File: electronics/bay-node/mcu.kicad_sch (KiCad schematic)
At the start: 15 parts, among them SW1 RESET, SW2 BOOT, U3 ESP32-S3-MINI-1-N8

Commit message: Bay node v0.5: 6-pin row cable with CAN and POS
The row cable becomes the docs/can.md contract: J1 (ROW IN, left) and J2 (ROW OUT,
right) are 6-pin JST PH S6B-PH-SM4-TB, +24 V, GND, CAN_H, CAN_L, GND, POS, with
pin 1 to the rear on the left edge and to the front on the right edge.

- Rack bus sheet: TCAN1044AV (VCC 5 V, VIO 3.3 V, STB low) right on the pair,
  which runs straight J1 -> J2 with no termination (stubs 1.8 / 2.3 mm),
  PESD2CAN on the tap; POS in through 10k + BAT54S + 100k pull-down, POS out
  through 10k + BAT54S.  TWAI on IO18/IO17, POS on IO16 (in) and IO35 (out).
- The input stage also takes a 20 / 28 V USB-C PD supply (notes on the Power
  sheet and in docs/electronics.md).
- Re-placed for In2 power only and autorouted: ERC 0, DRC 0, unconnected 0,
  parity 0 (kicad-cli and Konnect); no track on In1 or In2.
- JLC_CPL_FIX gains the rack bus parts, fitted on the EasyEDA footprints:
  S6B 180 deg, TCAN1044AV 270 deg, PESD2CAN and BAT54S 180 deg (they also apply
  to the power hub's row connectors, transceiver and clamps).
- Firmware: hwtr,rack-bus binding, TWAI pinctrl and node in the bay_node
  devicetree, check_pinmap and the README table; DevKitC moves POS_OUT to IO21,
  StampS3 disables the bus.  bay_node, DevKitC and StampS3 builds pass.
- Mechanics: the cable windows in the tray walls and the ladders widen to
  17 mm for the PHR-6 plug.  The viewer and the notice draw a 6-wire jumper.
- BOM: 6-pin jumpers; JLC_SINCE_QUOTE adds rev 0.5's parts and three extended
  part types to the node's quoted order (indicative, re-quote).

Regenerated: KiCad project, fab outputs, renders, schematic PDF, viewer GLB,
tray and ladder STLs, parts.glb, rack.json, bom/*.

Co-Authored-By: Claude Opus 5.5 <noreply@anthropic.com>
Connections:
- net POS_IN: now reaches U3.20 (IO16)
- net CAN_RXD: now reaches U3.21 (IO17)
- net CAN_TXD: now reaches U3.22 (IO18)
- net POS_OUT: now reaches U3.31 (IO35)
- no-connect marks 22 -> 18
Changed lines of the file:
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@@
 	(title_block
 		(title "Bay node — ESP32-S3 module")
-		(rev "0.4")
+		(rev "0.5")
 		(company "hw-testing-rack")
 		(comment 1 "ESP32-S3 USB/IP host for one bay of the hw-testing-rack shelf")
 		(comment 2 "Generated from electronics/bay-node/design.py — edit the Python, then regenerate")
-		(comment 3 "24 V in · 5 V/1.4 A switched DUT port · USB 2.0 muxes · INA226 · AUX UART/RST/BOOT")
+		(comment 3 "Row bus 20–28 V + CAN + POS in/out · 5 V/1.4 A switched DUT port · USB 2.0 muxes · INA226 · AUX")
 	)
 	(symbol
@@
 		)
 	)
-	(no_connect
-		(at 187.96 116.84)
+	(wire
+		(pts
+			(xy 187.96 116.84)
+			(xy 185.42 116.84)
+		)
+		(stroke
+			(width 0)
+			(type default)
+		)
 	)
-	(no_connect
-		(at 187.96 119.38)
+	(global_label "POS_IN"
+		(shape bidirectional)
+		(at 185.42 116.84 180)
+		(fields_autoplaced yes)
+		(effects
+			(font
+				(size 1.27 1.27)
+			)
+			(justify right)
+		)
+		(property "Intersheetrefs" "${INTERSHEET_REFS}"
+			(at 185.42 116.84 0)
+			(effects
+				(font
+					(size 1.27 1.27)
+				)
+				(justify right)
+				(hide yes)
+			)
+		)
 	)
-	(no_connect
-		(at 187.96 121.92)
+	(wire
+		(pts
+			(xy 187.96 119.38)
+			(xy 185.42 119.38)
+		)
+		(stroke
+			(width 0)
+			(type default)
+		)
+	)
+	(global_label "CAN_RXD"
+		(shape bidirectional)
+		(at 185.42 119.38 180)
+		(fields_autoplaced yes)
+		(effects
+			(font
+				(size 1.27 1.27)
+			)
+			(justify right)
+		)
+		(property "Intersheetrefs" "${INTERSHEET_REFS}"
+			(at 185.42 119.38 0)
+			(effects
+				(font
+					(size 1.27 1.27)
+				)
+				(justify right)
+				(hide yes)
+			)
+		)
+	)
+	(wire
+		(pts
+			(xy 187.96 121.92)
+			(xy 185.42 121.92)
+		)
+		(stroke
+			(width 0)
+			(type default)
+		)
+	)
+	(global_label "CAN_TXD"
+		(shape bidirectional)
+		(at 185.42 121.92 180)
+		(fields_autoplaced yes)
+		(effects
+			(font
+				(size 1.27 1.27)
+			)
+			(justify right)
+		)
+		(property "Intersheetrefs" "${INTERSHEET_REFS}"
+			(at 185.42 121.92 0)
+			(effects
+				(font
+					(size 1.27 1.27)
+				)
+				(justify right)
+				(hide yes)
+			)
+		)
 	)
 	(wire
@@
 		)
 	)
-	(no_connect
-		(at 218.44 93.98)
+	(wire
+		(pts
+			(xy 218.44 93.98)
+			(xy 220.98 93.98)
+		)
+		(stroke
+			(width 0)
+			(type default)
+		)
+	)
+	(global_label "POS_OUT"
+		(shape bidirectional)
+		(at 220.98 93.98 0)
+		(fields_autoplaced yes)
+		(effects
+			(font
+				(size 1.27 1.27)
+			)
+			(justify left)
+		)
+		(property "Intersheetrefs" "${INTERSHEET_REFS}"
+			(at 220.98 93.98 0)
+			(effects
+				(font
+					(size 1.27 1.27)
+				)
+				(justify left)
+				(hide yes)
+			)
+		)
 	)
 	(no_connect
@@
 		)
 	)
-	(text_box "GPIO map: IO41 DUT_EN · IO40 DUT_FLT_N · IO39 INA_ALERT · IO38/37 I2C SDA/SCL · IO47/33 UART1 TX/RX (AUX) ·\nIO34 AUX_RST · IO48 AUX_BOOT · IO12 LED · IO13 PC_DET · IO14 MUX_FORCE_PC · IO15 SVC · IO19/20 USB (OTG/JTAG).\nStrapping pins IO0/IO3/IO45/IO46 are not used for I/O.  USB is full-speed only (one internal PHY)."
+	(text_box "GPIO map: IO41 DUT_EN · IO40 DUT_FLT_N · IO39 INA_ALERT · IO38/37 I2C SDA/SCL · IO47/33 UART1 TX/RX (AUX) ·\nIO34 AUX_RST · IO48 AUX_BOOT · IO12 LED · IO13 PC_DET · IO14 MUX_FORCE_PC · IO15 SVC · IO19/20 USB (OTG/JTAG) ·\nIO18/17 CAN TX/RX (TWAI) · IO16 POS_IN · IO35 POS_OUT.\nStrapping pins IO0/IO3/IO45/IO46 are not used for I/O.  USB is full-speed only (one internal PHY)."
 		(exclude_from_sim no)
 		(at 15.24 177.8 0)
-		(size 269.24 11.43)
+		(size 269.24 13.97)
 		(margins 1.5 1.5 1.5 1.5)
 		(stroke

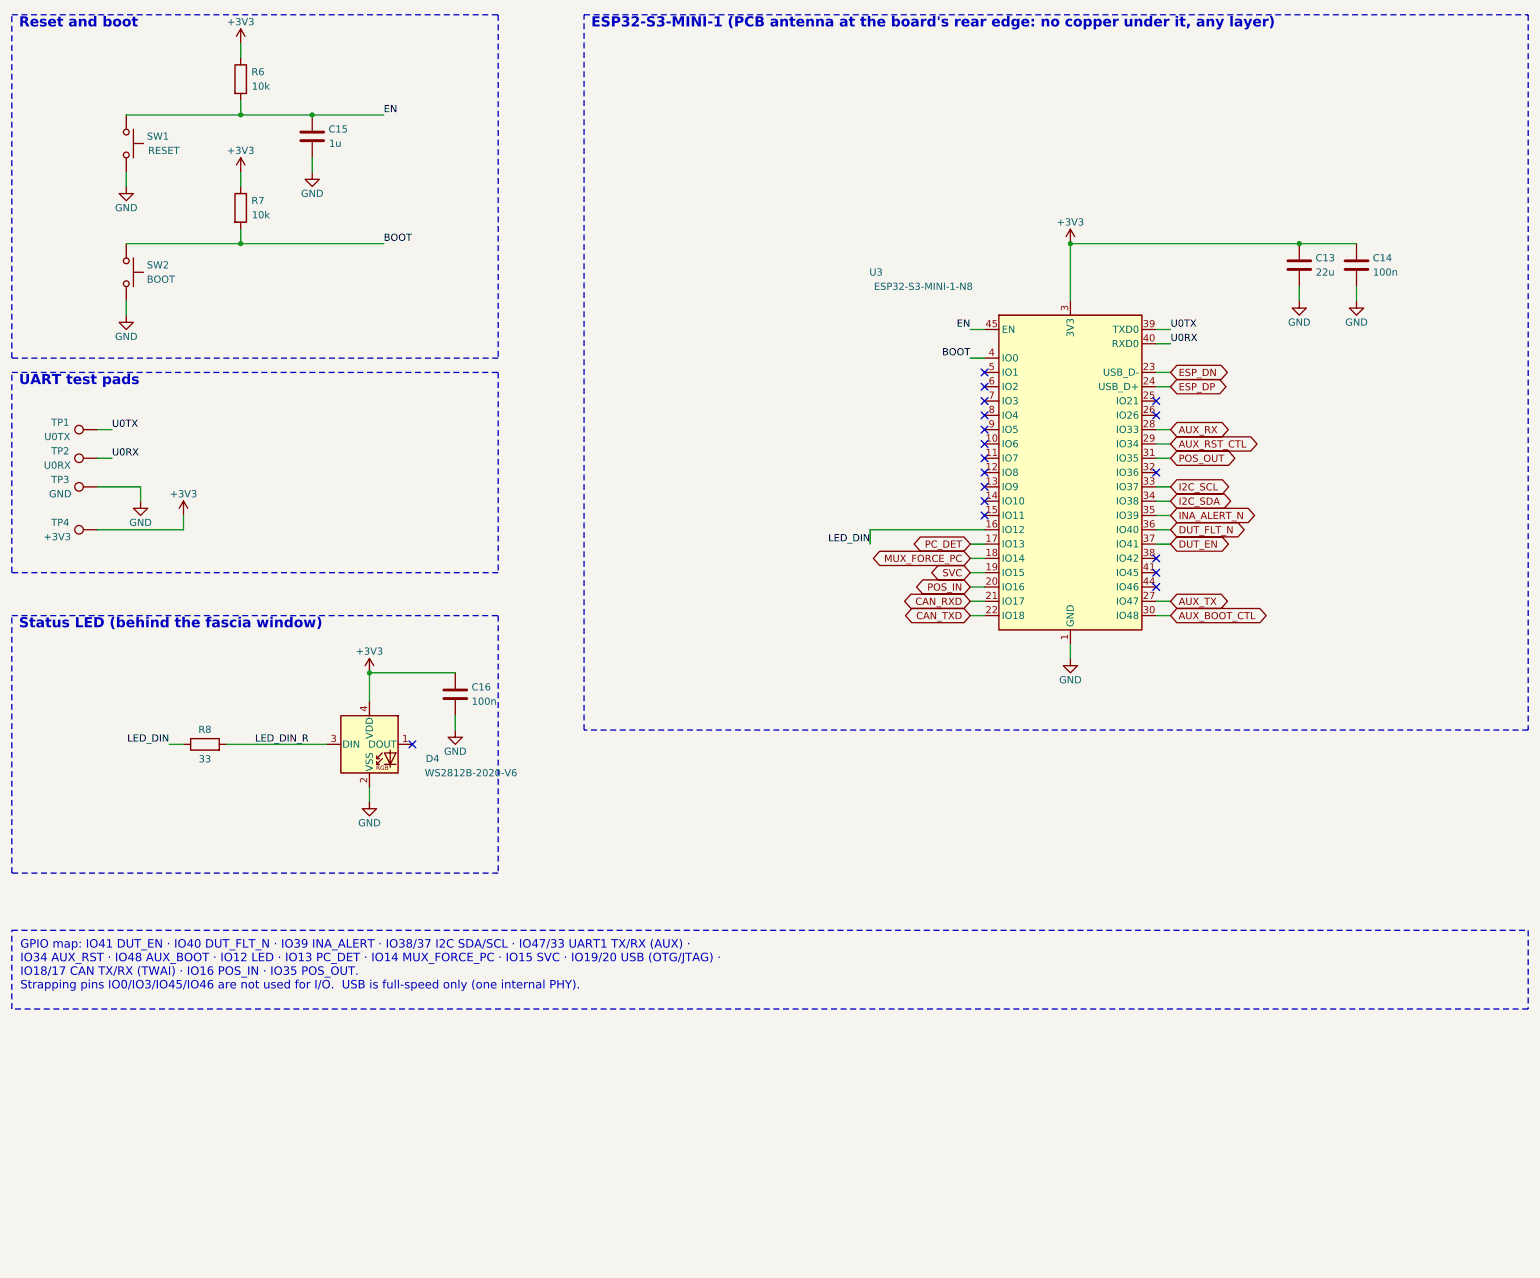
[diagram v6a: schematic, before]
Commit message: Bay node: the bay's camera on J6, the WROOM-1-N8R8, the board 64 × 90
The user chose a camera per bay wired to its own node (camera hand-over,
option B: an Arducam Mega 3MP SPI, M12 ≈ 120°, and white LEDs on one PH 8
lead) and the ESP32-S3-WROOM-1-N8R8 for its 8 MB octal PSRAM, allowing
the board to grow at the rear.

- U3: WROOM-1-N8R8 (C2913201), the DevKitC-1-N8R8's module.  The board
  grew 10 mm at the rear (64 × 90): the layout, the holes and every
  pcb.bay_node y moved 10 mm with it, so the tray's standoffs and the
  fascia parts keep their place; the module's top edge is the new rear
  edge, its antenna band (6 mm, ±24 mm) kept clear.  bench footprint
  ESP32-S3-WROOM-1_NoEPVias: the stock one without its 0.2 mm in-pad
  vias, the pad on a GND island stitched around it.
- Pin map (the PSRAM takes IO35–37, no IO26/33/34 on a WROOM-1), the
  DevKitC-1 v1.1's as is: IO1/IO2 I²C, IO12 AUX_RST, IO21 AUX_RX, IO38 LED,
  IO42 POS_OUT; camera IO11 SCK, IO10 MOSI, IO9 MISO, IO8 CS, IO7 light.
- J6: PH 8 vertical (B8B) right of the PC pair, under J7; 33 Ω series,
  2 × USBLC6, CS 10k pull-up, MISO divider footprint (R35 DNP), the light
  on an AO3400A (100k gate pull-down), CAM_5V through the PTC.  A
  "Camera" schematic sheet.
- J5 (AUX): a vertical PH 6 (B6B), as the user asked.
- Re-routed.  ERC 0, DRC 0 / 0 unconnected / parity 0, JLC DFM: only the
  back-side test pads, 97/97 3D models (the B6B's EasyEDA STEP is not
  centred and turned).  The session import now also drops a via at the
  end of a dead branch, and the branch.  JLC corrections fitted for
  C2913201, C495548, C471518, C20917.
- BOM: the camera lines (B0434, 120° lens, LED strip, PH 8 lead) replace
  the XIAO / OV2640 / PH 2 lead; the node's post-quote changes +$18.91
  of parts, +$3 for the B6B type, +$1.83 for the larger board.
- firmware/README.md pin map: the new map.  check_pinmap waits for the
  firmware's devicetree (moved pins, camera).

Co-Authored-By: Claude Opus 5.5 <noreply@anthropic.com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
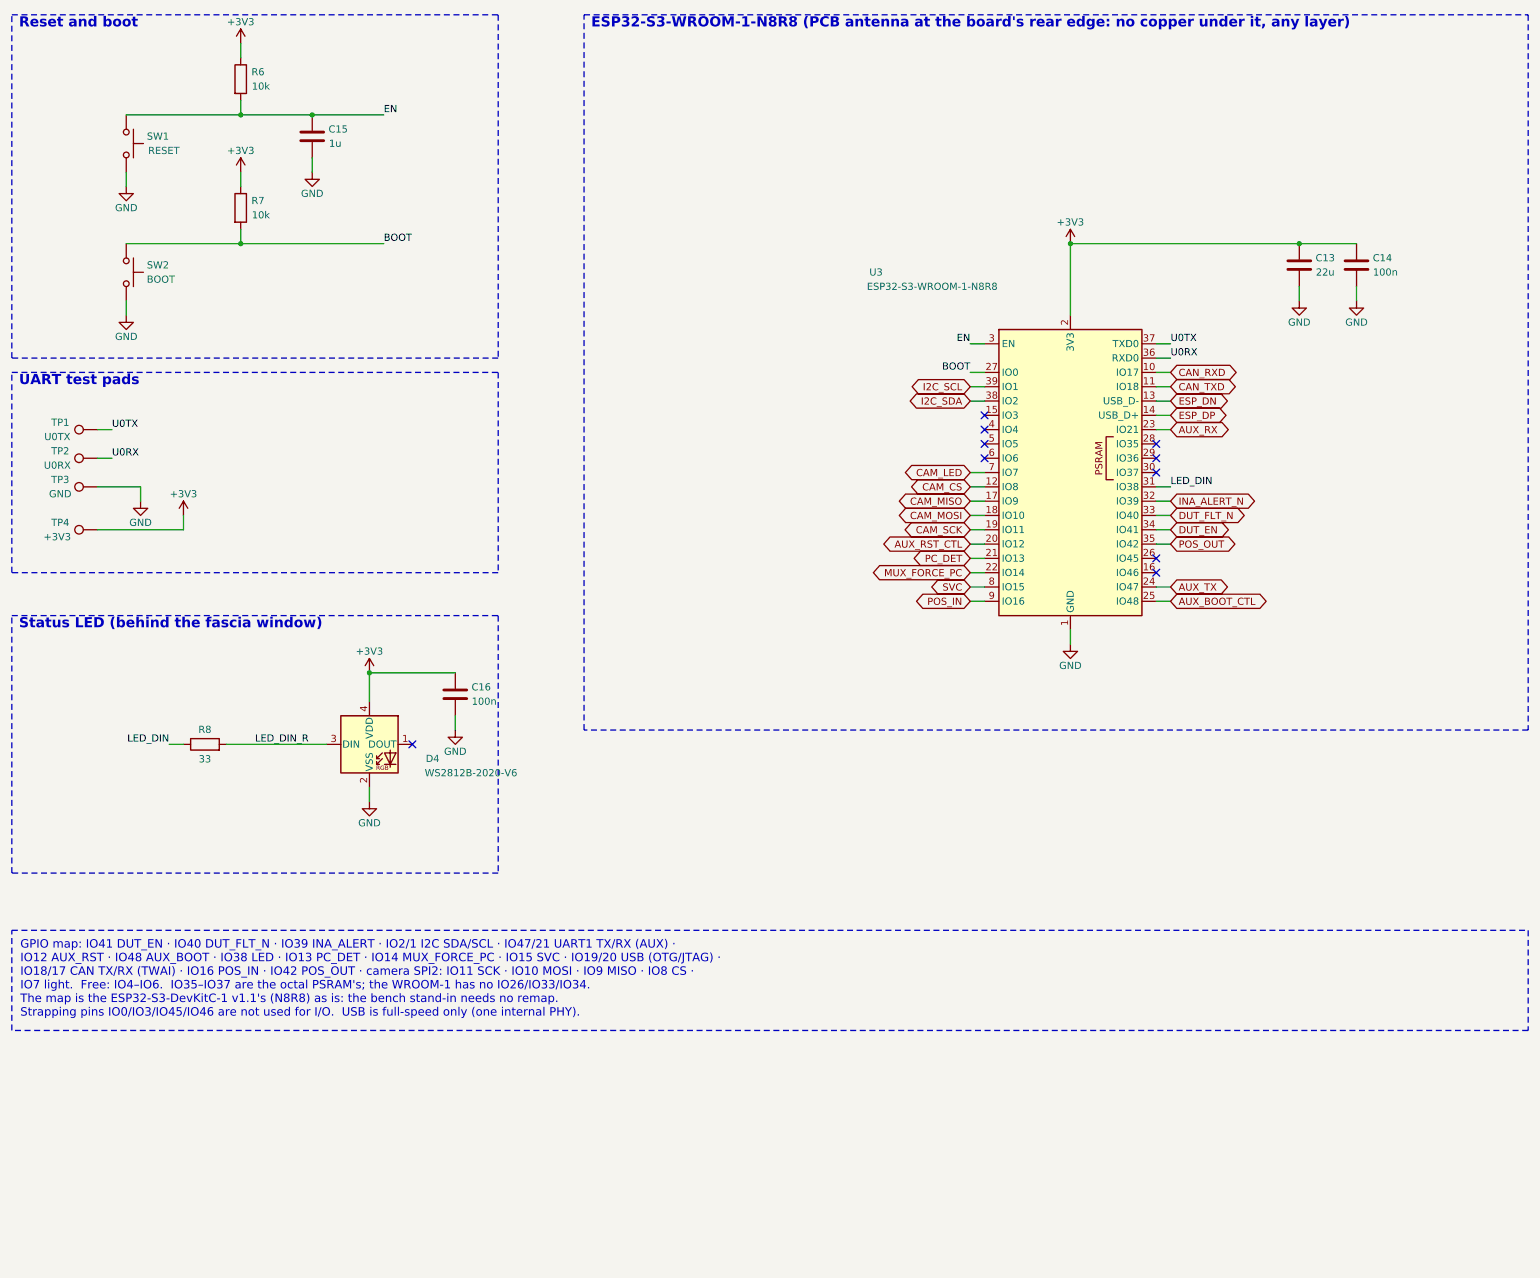
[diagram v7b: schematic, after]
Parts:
- U3: value ESP32-S3-MINI-1-N8 -> ESP32-S3-WROOM-1-N8R8; footprint RF_Module:ESP32-S2-MINI-1 -> bench:ESP32-S3-WROOM-1_NoEPVias; symbol RF_Module:ESP32-S3-MINI-1 -> RF_Module:ESP32-S3-WROOM-1; LCSC C2913206 -> C2913201; MPN ESP32-S3-MINI-1-N8 -> ESP32-S3-WROOM-1-N8R8
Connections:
- net +3V3: now also U3.2 (3V3); no longer U3.3 (3V3)
- net AUX_BOOT_CTL: now also U3.25 (IO48); no longer U3.30 (IO48)
- net AUX_RST_CTL: now also U3.20 (IO12); no longer U3.29 (IO34)
- net AUX_RX: now also U3.23 (IO21); no longer U3.28 (IO33)
- net AUX_TX: now also U3.24 (IO47); no longer U3.27 (IO47)
- net BOOT: now also U3.27 (IO0); no longer U3.4 (IO0)
- net CAN_RXD: now also U3.10 (IO17); no longer U3.21 (IO17)
- net CAN_TXD: now also U3.11 (IO18); no longer U3.22 (IO18)
- net DUT_EN: now also U3.34 (IO41); no longer U3.37 (IO41)
- net DUT_FLT_N: now also U3.33 (IO40); no longer U3.36 (IO40)
- net EN: now also U3.3 (EN); no longer U3.45 (EN)
- net ESP_DN: now also U3.13 (USB_D-); no longer U3.23 (USB_D-)
- net ESP_DP: now also U3.14 (USB_D+); no longer U3.24 (USB_D+)
- net GND: now also U3.40 (GND), U3.41 (GND); no longer U3.2 (GND), U3.42 (GND), U3.43 (GND), U3.46 (GND), U3.47 (GND), U3.48 (GND), U3.49 (GND), U3.50 (GND), U3.51 (GND), U3.52 (GND), U3.53 (GND), U3.54 (GND), U3.55 (GND), U3.56 (GND), U3.57 (GND), U3.58 (GND), U3.59 (GND), U3.60 (GND), U3.61 (GND), U3.62 (GND), U3.63 (GND), U3.64 (GND), U3.65 (GND)
- net I2C_SCL: now also U3.39 (IO1); no longer U3.33 (IO37)
- net I2C_SDA: now also U3.38 (IO2); no longer U3.34 (IO38)
- net INA_ALERT_N: now also U3.32 (IO39); no longer U3.35 (IO39)
- net LED_DIN: now also U3.31 (IO38); no longer U3.16 (IO12)
- net MUX_FORCE_PC: now also U3.22 (IO14); no longer U3.18 (IO14)
- net PC_DET: now also U3.21 (IO13); no longer U3.17 (IO13)
- net POS_IN: now also U3.9 (IO16); no longer U3.20 (IO16)
- net POS_OUT: now also U3.35 (IO42); no longer U3.31 (IO35)
- net SVC: now also U3.8 (IO15); no longer U3.19 (IO15)
- net U0RX: now also U3.36 (RXD0); no longer U3.40 (RXD0)
- net U0TX: now also U3.37 (TXD0); no longer U3.39 (TXD0)
- net CAM_CS: now reaches U3.12 (IO8)
- net CAM_LED: now reaches U3.7 (IO7)
- new net CAM_MISO: U3.17 (IO9)
- new net CAM_MOSI: U3.18 (IO10)
- new net CAM_SCK: U3.19 (IO11)
- no-connect marks 18 -> 10
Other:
- note added: "ESP32-S3-WROOM-1-N8R8 (PCB antenna at the board's rear edge: no copper under it, any layer)"
- note removed: "ESP32-S3-MINI-1 (PCB antenna at the board's rear edge: no copper under it, any layer)"

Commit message: DATA lead on 8 wires: node J7 a vertical PH 8 (USB, I²C, INT), data port J2 an S8B
Density decisions of 2026-10-19: the DATA lead becomes the camera's PH 8
"Same direction" type and also carries the node's I²C and an open-drain,
active-low INT (IO4, 10k pull-up, 1k at J7) for a later DATA ×4 board.

- Node: J7 B8B vertical by the right edge (J5's old slot), J5 AUX
  horizontal in the middle, AUX parts in a column between them.  J7 now
  taps the pair at J4's pads (DUT_CONN_*, behind U8's ESD like J4); the
  branch is hand-drawn in usb_hs_routes() on B.Cu under J4, since
  Freerouting found no room on U8's mux side.  ERC 0, DRC 0, parity 0,
  99 models.
- Data port: S8B, pins 1–3 open, PH at x 14.4, left hole (2.6, 13.5),
  one silkscreen label per pin.  ERC 0, DRC 0, parity 0.
- Pin map (README, check_pinmap: DATA_INT reserved), docs, cabling,
  BOM (one PH 8 lead type for DATA and camera, no B5B/S5B), SCAD config.

Co-Authored-By: Claude Opus 5.5 <noreply@anthropic.com>
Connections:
- net DATA_INT: now reaches U3.4 (IO4)
- no-connect marks 10 -> 9
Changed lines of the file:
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@@
 		)
 	)
-	(no_connect
-		(at 187.96 88.9)
+	(wire
+		(pts
+			(xy 187.96 88.9)
+			(xy 185.42 88.9)
+		)
+		(stroke
+			(width 0)
+			(type default)
+		)
+	)
+	(global_label "DATA_INT"
+		(shape bidirectional)
+		(at 185.42 88.9 180)
+		(fields_autoplaced yes)
+		(effects
+			(font
+				(size 1.27 1.27)
+			)
+			(justify right)
+		)
+		(property "Intersheetrefs" "${INTERSHEET_REFS}"
+			(at 185.42 88.9 0)
+			(effects
+				(font
+					(size 1.27 1.27)
+				)
+				(justify right)
+				(hide yes)
+			)
+		)
 	)
 	(no_connect
@@
 		)
 	)
-	(text_box "GPIO map: IO41 DUT_EN · IO40 DUT_FLT_N · IO39 INA_ALERT · IO2/1 I2C SDA/SCL · IO47/21 UART1 TX/RX (AUX) ·\nIO12 AUX_RST · IO48 AUX_BOOT · IO38 LED · IO13 PC_DET · IO14 MUX_FORCE_PC · IO15 SVC · IO19/20 USB (OTG/JTAG) ·\nIO18/17 CAN TX/RX (TWAI) · IO16 POS_IN · IO42 POS_OUT · camera SPI2: IO11 SCK · IO10 MOSI · IO9 MISO · IO8 CS ·\nIO7 light.  Free: IO4–IO6.  IO35–IO37 are the octal PSRAM's; the WROOM-1 has no IO26/IO33/IO34.\nThe map is the ESP32-S3-DevKitC-1 v1.1's (N8R8) as is: the bench stand-in needs no remap.\nStrapping pins IO0/IO3/IO45/IO46 are not used for I/O.  USB is full-speed only (one internal PHY)."
+	(text_box "GPIO map: IO41 DUT_EN · IO40 DUT_FLT_N · IO39 INA_ALERT · IO2/1 I2C SDA/SCL · IO47/21 UART1 TX/RX (AUX) ·\nIO12 AUX_RST · IO48 AUX_BOOT · IO38 LED · IO13 PC_DET · IO14 MUX_FORCE_PC · IO15 SVC · IO19/20 USB (OTG/JTAG) ·\nIO18/17 CAN TX/RX (TWAI) · IO16 POS_IN · IO42 POS_OUT · camera SPI2: IO11 SCK · IO10 MOSI · IO9 MISO · IO8 CS ·\nIO7 light · IO4 DATA_INT (J7.8, open drain, active low).  Free: IO5, IO6.  IO35–IO37 are the octal PSRAM's;\nthe WROOM-1 has no IO26/IO33/IO34.  The I²C bus (IO1/IO2) also goes out on J7.6/7 to the drawer's DATA board.\nThe map is the ESP32-S3-DevKitC-1 v1.1's (N8R8) as is: the bench stand-in needs no remap.\nStrapping pins IO0/IO3/IO45/IO46 are not used for I/O.  USB is full-speed only (one internal PHY)."
 		(exclude_from_sim no)
 		(at 15.24 177.8 0)
-		(size 269.24 17.78)
+		(size 269.24 20.32)
 		(margins 1.5 1.5 1.5 1.5)
 		(stroke
